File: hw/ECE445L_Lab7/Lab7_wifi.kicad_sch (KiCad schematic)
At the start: 4 parts, among them U1 ESP8266-1

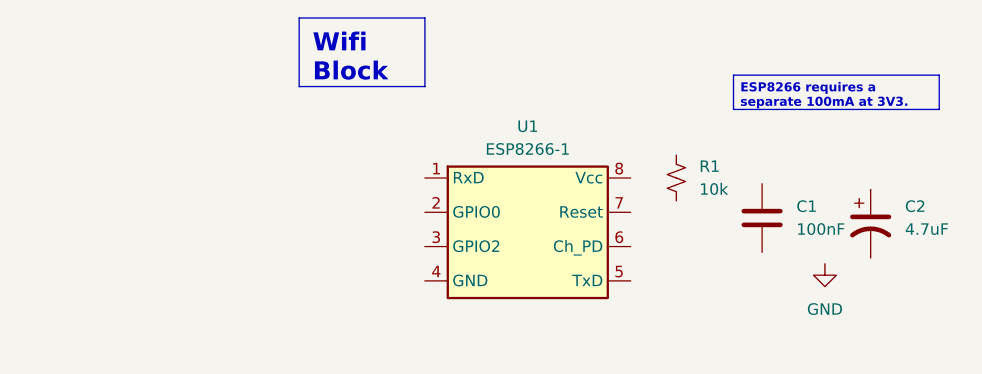
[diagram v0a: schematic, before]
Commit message: added reverse engineering for water atomizer
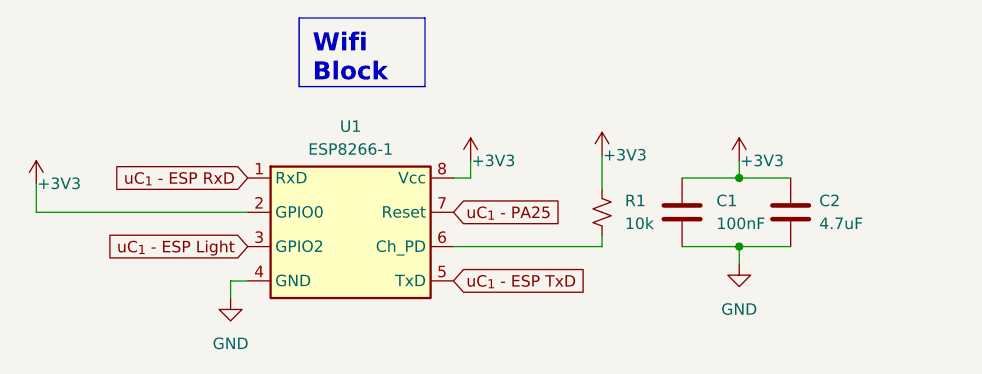
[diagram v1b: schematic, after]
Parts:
- C2: symbol ECE445L:C_Polarized -> Device:C
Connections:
- net GND: now also C1.2, C2.2, U1.4 (GND)
- net uC_{1} - ESP RxD: now reaches U1.1 (RxD)
- net +3V3: now reaches U1.2 (GPIO0)
- net +3V3: now also C1.1, C2.1, R1.1, U1.8 (Vcc)
- net uC_{1} - ESP Light: now reaches U1.3 (GPIO2)
- net uC_{1} - ESP TxD: now reaches U1.5 (TxD)
- net at U1.6 (Ch_PD): now also R1.2
- net uC_{1} - PA25: now reaches U1.7 (Reset)
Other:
- company: (none) -> ECE445L
- moved on the sheet: C1, R1, U1

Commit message: almost finished with schem
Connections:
- net uC_{1} - PA25 renamed uC_{1} - ESP RST
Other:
- note added: "ESP8266 Module"
- moved on the sheet: C1, C2, R1, U1

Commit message: finished prelim schem
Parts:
- C_{b}16: renamed from C1; value 100nF -> 100n; footprint ECE445L:C_Radial_100mil -> Capacitor_SMD:C_0603_1608Metric_Pad1.08x0.95mm_HandSolder; Distributor (none) -> Mouser; Manufacturer (none) -> Walsin; Manufacturer_Part_Number (none) -> 0603B104J160CT; Mouser Part Number (none) -> 791-0603B104J160CT
- C_{b}17: renamed from C2; value 4.7uF -> 4.7u; footprint ECE445L:CP_Radial_Tantal200mil -> Capacitor_SMD:C_0603_1608Metric_Pad1.08x0.95mm_HandSolder; Distributor (none) -> Mouser; Manufacturer (none) -> Walsin; Manufacturer_Part_Number (none) -> 0805X475M250CT; Mouser Part Number (none) -> 791-0805X475M250CT
- ESP8266: renamed from U1; Distributor (none) -> 445L
- R_{PU}1: renamed from R1; footprint ECE445L:R_Axial_DIN0204_L3.6mm_D1.6mm_P7.62mm_Horizontal -> Resistor_SMD:R_0805_2012Metric_Pad1.20x1.40mm_HandSolder; Distributor (none) -> Mouser; Manufacturer (none) -> Bourns; Manufacturer_Part_Number (none) -> CRM0805-FX-1002ELF; Mouser Part Number (none) -> 652-CRM0805FX1002ELF
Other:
- moved on the sheet: C_{b}16, C_{b}17

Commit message: handoff to jonathan until midnight
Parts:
- C_{b}17, R_{PU}1: Distributor Mouser -> Valvano
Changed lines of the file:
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@@
 			)
 		)
-		(property "Distributor" "Mouser"
+		(property "Distributor" "Valvano"
 			(at 194.31 96.52 0)
 			(hide yes)
@@
 			)
 		)
-		(property "Distributor" "Mouser"
+		(property "Distributor" "Valvano"
 			(at 172.085 96.52 0)
 			(hide yes)
